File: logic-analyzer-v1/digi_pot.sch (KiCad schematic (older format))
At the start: 5 parts

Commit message: add comparator&sram
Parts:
- U?: symbol Potentiometer_Digital:MCP4551 -> logic-analyzer-v1-rescue:MCP4551-Potentiometer_Digital
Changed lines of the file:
@@
 $EndComp
 $Comp
-L Potentiometer_Digital:MCP4551 U?
+L logic-analyzer-v1-rescue:MCP4551-Potentiometer_Digital U?
 U 1 1 5FDA8C94
 P 5150 3300

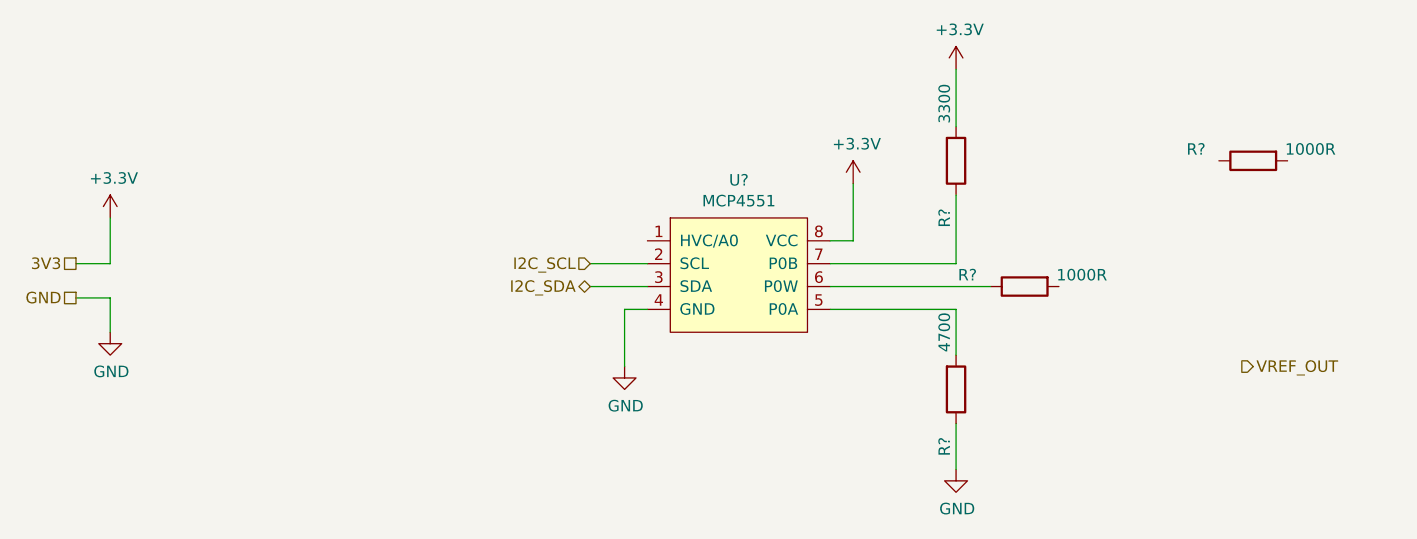
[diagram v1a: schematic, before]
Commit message: MOD uart port direction, minor cosmetic changes
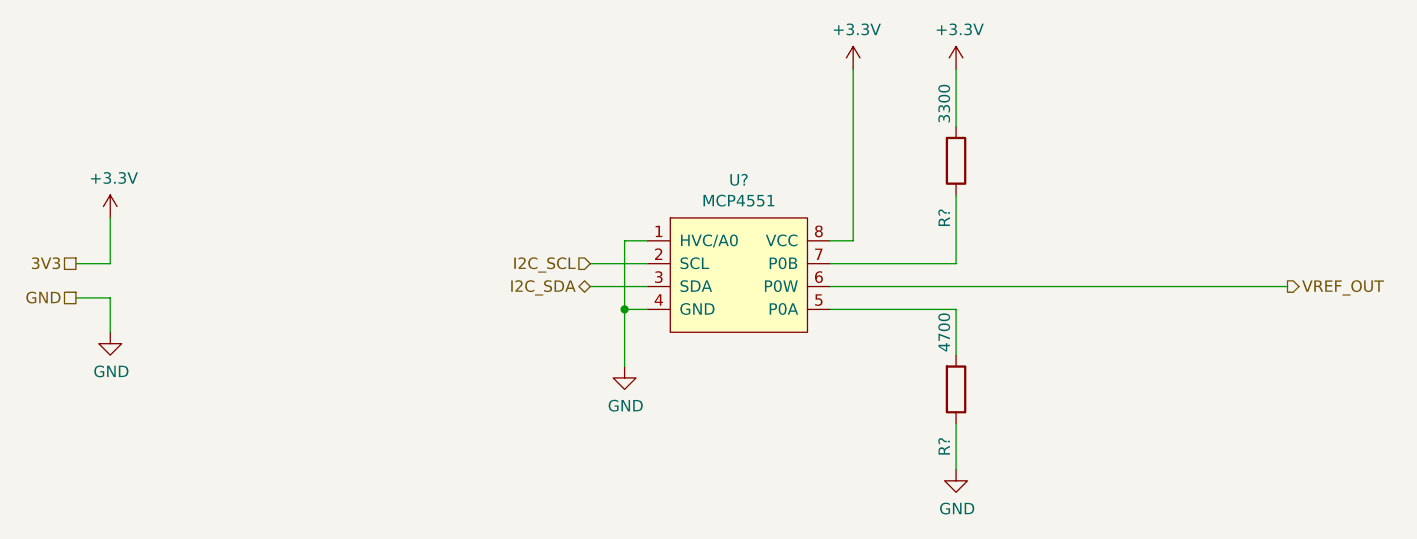
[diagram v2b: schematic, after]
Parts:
- removed R? (x2): 1000R, Resistor_SMD:R_0603_1608Metric_Pad1.05x0.95mm_HandSolder, symbol Device:R
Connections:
- net GND: now also U?.1 (HVC/A0)
- net VREF_OUT: now also U?.6 (P0W)
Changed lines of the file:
@@
 $Descr A4 11693 8268
 encoding utf-8
-Sheet 4 6
+Sheet 4 8
 Title ""
 Date ""
@@
 Comment4 ""
 $EndDescr
-Text HLabel 7350 3950 2    50   Output ~ 0
+Text HLabel 7550 3600 2    50   Output ~ 0
 VREF_OUT
 Text HLabel 2250 3500 0    50   UnSpc ~ 0
@@
 	4500 3500 4750 3500
 $Comp
-L Device:R R?
-U 1 1 5FDF9C45
-P 6400 3600
-AR Path="/5F08ED8D/5FDF9C45" Ref="R?"  Part="1"
-AR Path="/5F19654C/5FDF9C45" Ref="R?"  Part="1"
-AR Path="/5FDA887A/5FDA8D6E/5FDF9C45" Ref="R?"  Part="1"
-F 0 "R?" V 6350 3850 50  0000 C CNN
-F 1 "1000R" V 6350 3350 50  0000 C CNN
-F 2 "Resistor_SMD:R_0603_1608Metric_Pad1.05x0.95mm_HandSolder" V 6330 3600 50  0001 C CNN
-F 3 "~" H 6400 3600 50  0001 C CNN
-	1    6400 3600
-	0    -1   1    0
-$EndComp
-$Comp
-L Device:R R?
-U 1 1 5FDFA1CA
-P 7400 3050
-AR Path="/5F08ED8D/5FDFA1CA" Ref="R?"  Part="1"
-AR Path="/5F19654C/5FDFA1CA" Ref="R?"  Part="1"
-AR Path="/5FDA887A/5FDA8D6E/5FDFA1CA" Ref="R?"  Part="1"
-F 0 "R?" V 7350 3300 50  0000 C CNN
-F 1 "1000R" V 7350 2800 50  0000 C CNN
-F 2 "Resistor_SMD:R_0603_1608Metric_Pad1.05x0.95mm_HandSolder" V 7330 3050 50  0001 C CNN
-F 3 "~" H 7400 3050 50  0001 C CNN
-	1    7400 3050
-	0    -1   1    0
-$EndComp
-$Comp
 L logic-analyzer-v1-rescue:MCP4551-Potentiometer_Digital U?
 U 1 1 5FDA8C94
@@
 L power:+3.3V #PWR?
 U 1 1 5FDA93EF
-P 5650 3150
-F 0 "#PWR?" H 5650 3000 50  0001 C CNN
-F 1 "+3.3V" H 5665 3323 50  0000 C CNN
-F 2 "" H 5650 3150 50  0001 C CNN
-F 3 "" H 5650 3150 50  0001 C CNN
-	1    5650 3150
+P 5650 2650
+F 0 "#PWR?" H 5650 2500 50  0001 C CNN
+F 1 "+3.3V" H 5665 2823 50  0000 C CNN
+F 2 "" H 5650 2650 50  0001 C CNN
+F 3 "" H 5650 2650 50  0001 C CNN
+	1    5650 2650
 	1    0    0    -1
 $EndComp
@@
 	5550 3400 5650 3400
 Wire Wire Line
-	5650 3400 5650 3150
+	5650 3400 5650 2650
 $Comp
 L power:+3.3V #PWR?
@@
 	5550 3700 6100 3700
 Wire Wire Line
-	5550 3600 6250 3600
+	4650 3700 4650 3400
+Wire Wire Line
+	4650 3400 4750 3400
+Connection ~ 4650 3700
+Wire Wire Line
+	5550 3600 7550 3600
 $EndSCHEMATC

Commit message: improvement origin in libraries and creation my_library containing all ours libraries
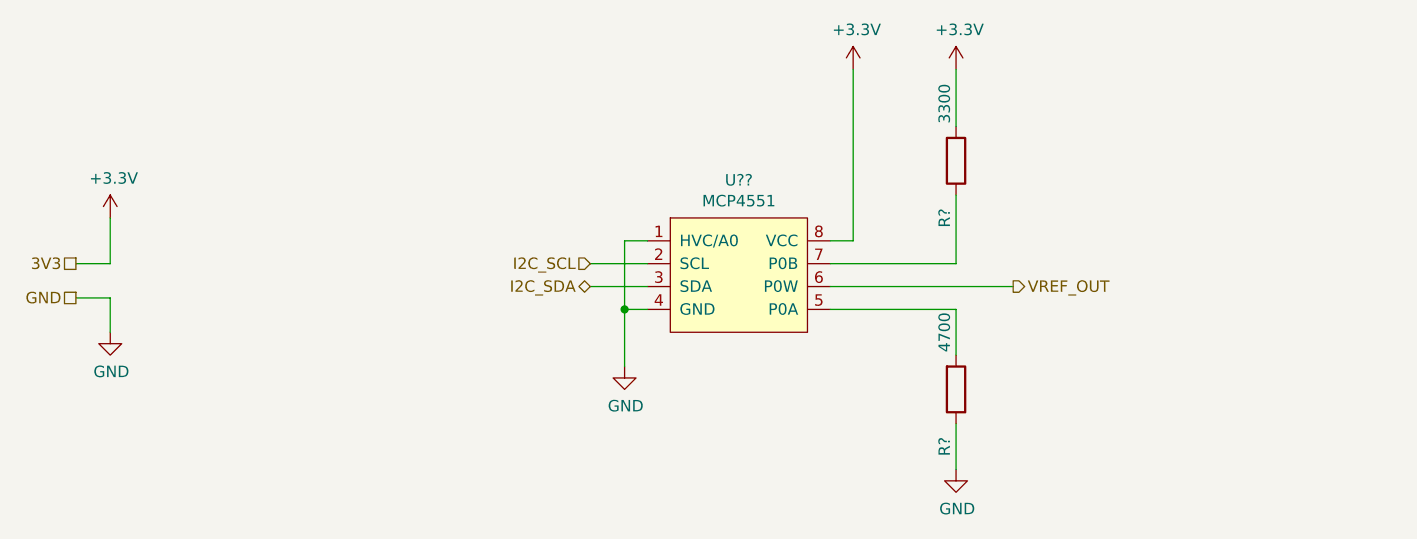
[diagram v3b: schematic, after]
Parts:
- removed U?: MCP4551, symbol logic-analyzer-v1-rescue:MCP4551-Potentiometer_Digital
- added U??: MCP4551, symbol my_library:MCP4551
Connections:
- net +3V3: now also U??.8 (VCC)
- net GND: now also U??.1 (HVC/A0), U??.4 (GND)
- net I2C_SCL: now also U??.2 (SCL)
- net I2C_SDA: now also U??.3 (SDA)
- net VREF_OUT: now also U??.6 (P0W)
- net at R?.2: now also U??.5 (P0A)
- net at R?.1: now also U??.7 (P0B)
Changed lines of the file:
@@
 Comment4 ""
 $EndDescr
-Text HLabel 7550 3600 2    50   Output ~ 0
+Text HLabel 6350 3600 2    50   Output ~ 0
 VREF_OUT
 Text HLabel 2250 3500 0    50   UnSpc ~ 0
@@
 Wire Wire Line
 	4500 3500 4750 3500
-$Comp
-L logic-analyzer-v1-rescue:MCP4551-Potentiometer_Digital U?
-U 1 1 5FDA8C94
-P 5150 3300
-F 0 "U?" H 5150 3465 50  0000 C CNN
-F 1 "MCP4551" H 5150 3374 50  0000 C CNN
-F 2 "" H 5200 3300 50  0001 C CNN
-F 3 "https://ww1.microchip.com/downloads/en/DeviceDoc/22096b.pdf" H 5200 3300 50  0001 C CNN
-	1    5150 3300
-	1    0    0    -1
-$EndComp
 $Comp
 L power:+3.3V #PWR?
@@
 Connection ~ 4650 3700
 Wire Wire Line
-	5550 3600 7550 3600
+	5550 3600 6350 3600
+$Comp
+L my_library:MCP4551 U??
+U 1 1 60879532
+P 5150 3550
+F 0 "U??" H 5150 3965 50  0000 C CNN
+F 1 "MCP4551" H 5150 3874 50  0000 C CNN
+F 2 "" H 5200 3800 50  0001 C CNN
+F 3 "https://ww1.microchip.com/downloads/en/DeviceDoc/22096b.pdf" H 5200 3800 50  0001 C CNN
+	1    5150 3550
+	1    0    0    -1
+$EndComp
 $EndSCHEMATC
